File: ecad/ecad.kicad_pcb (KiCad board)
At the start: 4 copper layers, 130.5 x 110 mm, 101 parts, among them J1 JTAG, J2 USB_C, J3 Display, SW1 Kailh choc v2, SW10 RotaryEncoder_Switch, SW11 RotaryEncoder_Switch, SW12 Kailh choc v2, SW13 Kailh choc v2, SW14 Kailh choc v2, SW15 RESET, SW16 Kailh choc v2, SW17 Kailh choc v2, SW18 Kailh choc v2, SW19 Kailh choc v2, SW2 Kailh choc v2, SW20 Kailh choc v2, SW21 Kailh choc v2, SW22 Kailh choc v2, SW23 Kailh choc v2, SW24 Kailh choc v2, SW25 Kailh choc v2, SW3 Kailh choc v2, SW4 Kailh choc v2, SW5 Kailh choc v2, SW6 Kailh choc v2, SW7 Kailh choc v2, SW8 Kailh choc v2, SW9 Kailh choc v2, U1 AP2112K-3.3, U2 RP2040, U4 SN74LV1T34DBV, U5 W25Q128JVP, Y1 12MHz

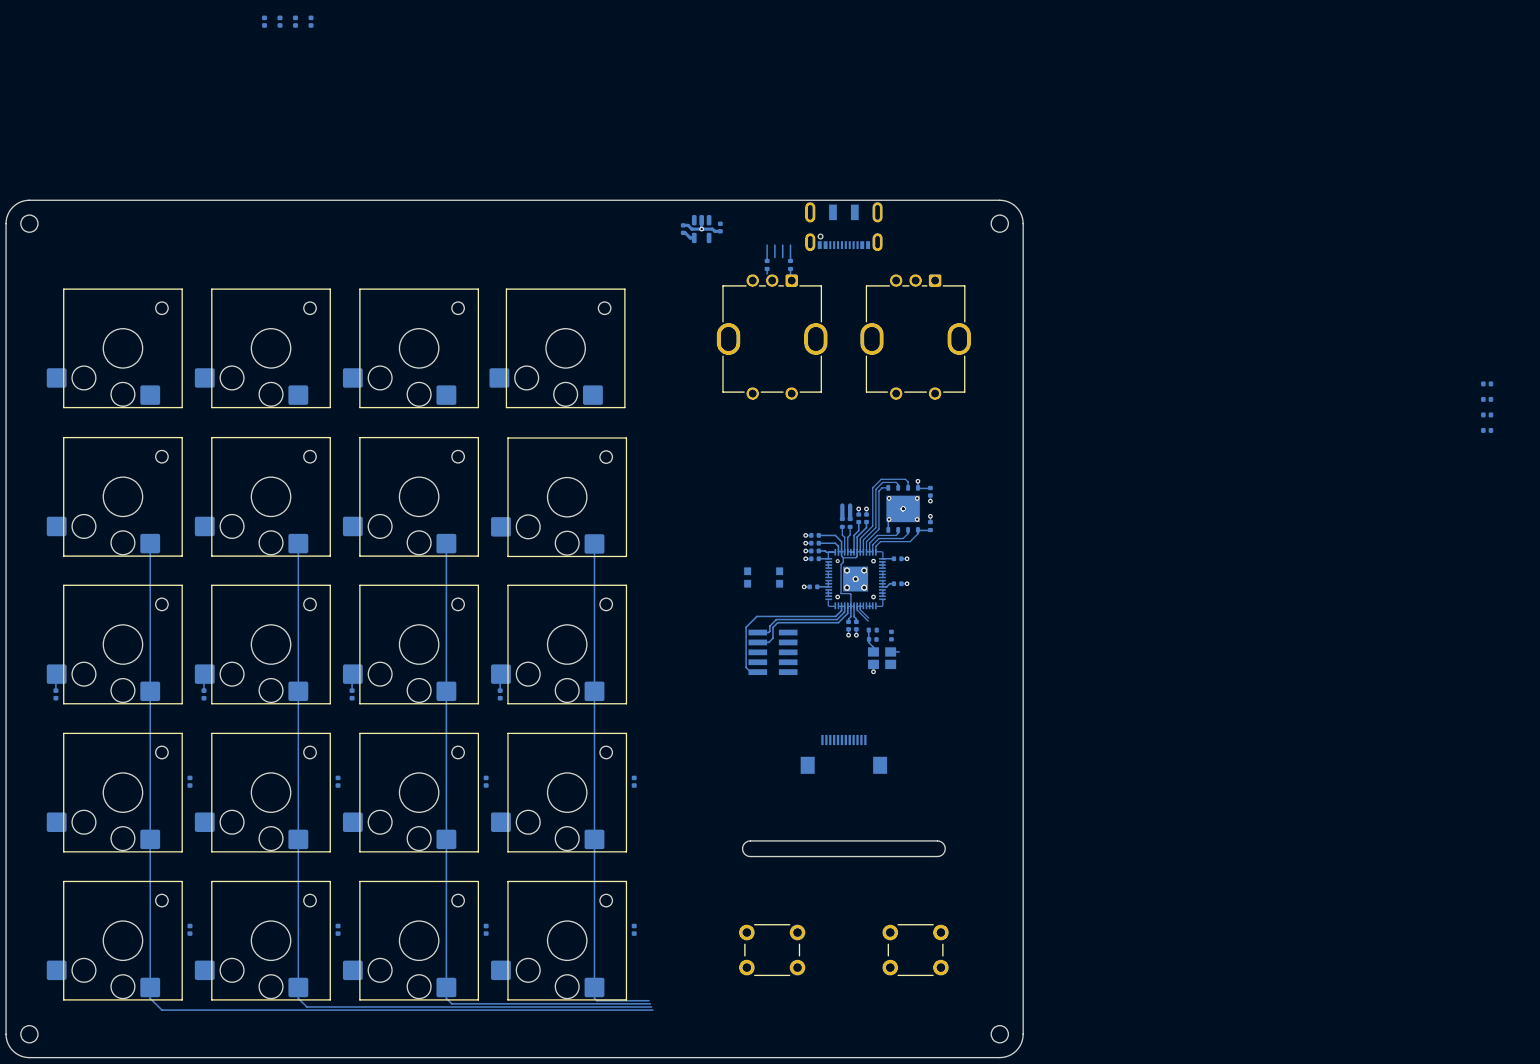
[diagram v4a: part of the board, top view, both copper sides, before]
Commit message: feat(ecad): hierarchical sheets, add switches net and change some components placement
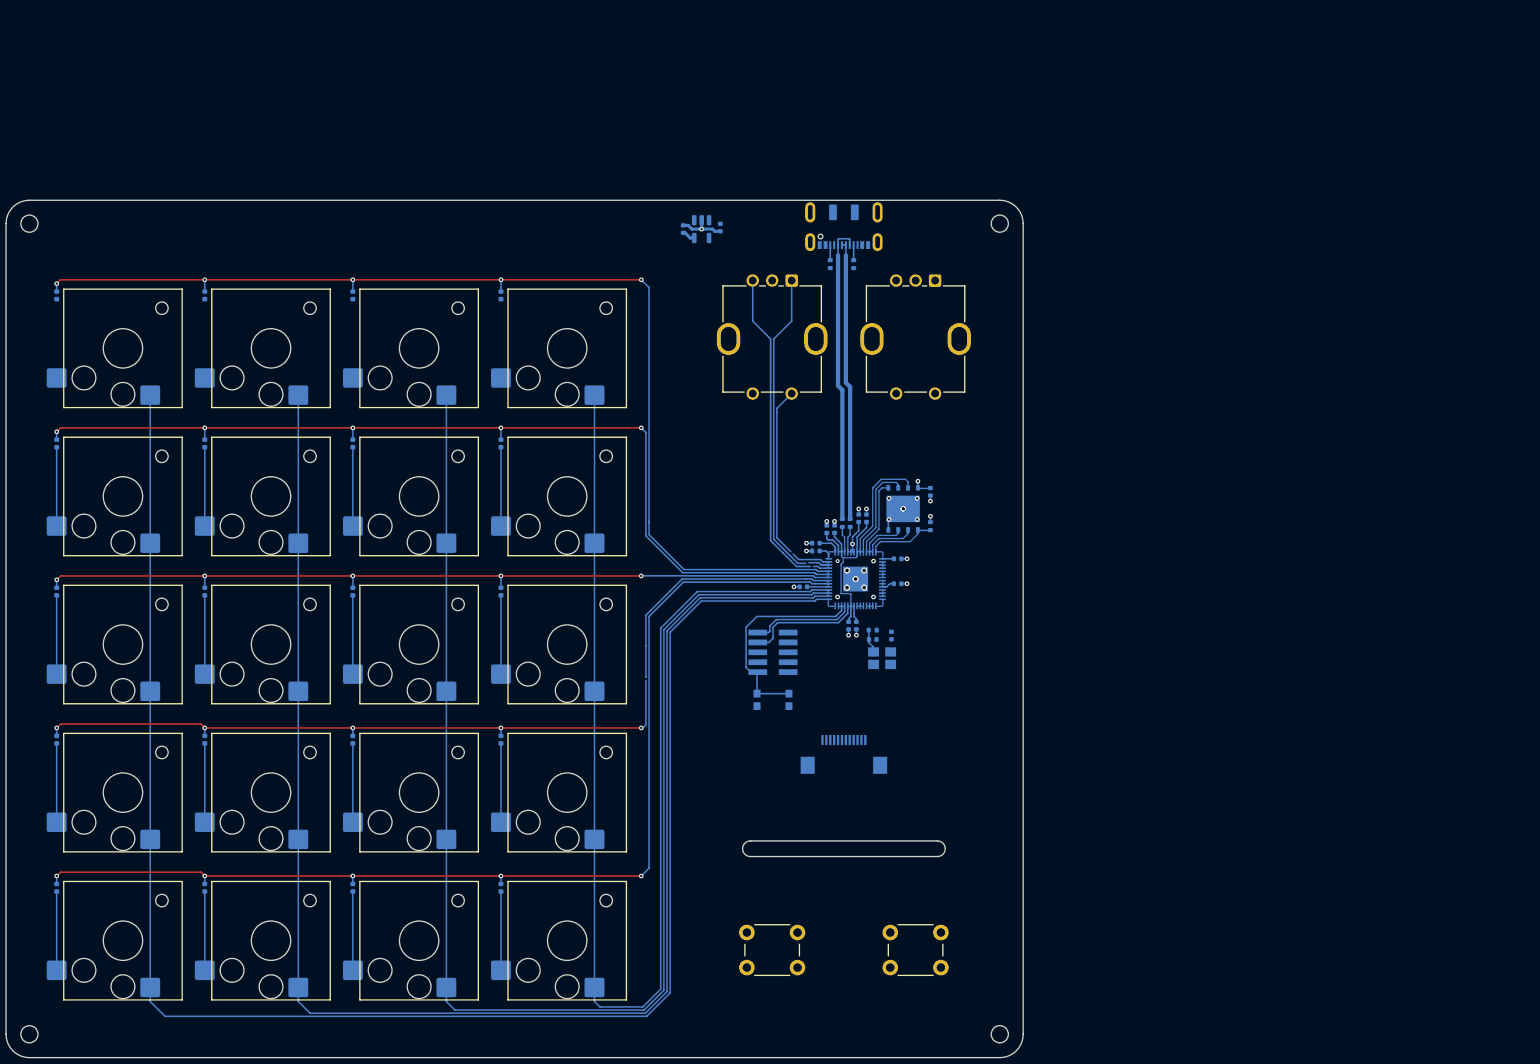
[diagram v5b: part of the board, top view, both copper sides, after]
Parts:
- moved D36 183.5 mm to (69.7, 99.1), turned to -90 degrees
- moved D35 164.6 mm to (88.7, 99.1), turned to -90 degrees
- moved D34 145.6 mm to (107.7, 99.1), turned to -90 degrees
- moved D33 126.8 mm to (126.7, 99.1), turned to -90 degrees
- moved D40 44.1 mm to (69.7, 80.1), turned to -90 degrees
- moved D37 42.7 mm to (126.7, 80.1), turned to -90 degrees
- moved D39 36.4 mm to (88.7, 80.1), turned to -90 degrees
- moved D38 35.9 mm to (107.7, 80.1), turned to -90 degrees
- moved D2 17.9 mm to (126.7, 137.1), turned to -90 degrees
- moved D3 17.9 mm to (126.7, 156.1), turned to -90 degrees
- moved D11 17.9 mm to (69.7, 137.1), turned to -90 degrees
- moved D12 17.9 mm to (69.7, 156.1), turned to -90 degrees
- moved D5 17.9 mm to (107.7, 137.1), turned to -90 degrees
- moved D6 17.9 mm to (107.7, 156.1), turned to -90 degrees
- moved D8 17.9 mm to (88.7, 137.1), turned to -90 degrees
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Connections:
- net /led/DIN renamed /Leds/DIN
- D1 pad 1: Net-(D1-K) -> /Switches/R3
- D10 pad 1: Net-(D1-K) -> /Switches/R3
- D11 pad 1: Net-(D11-K) -> /Switches/R4
- D12 pad 1: Net-(D12-K) -> /Switches/R5
- D2 pad 1: Net-(D11-K) -> /Switches/R4
- D3 pad 1: Net-(D12-K) -> /Switches/R5
- D33 pad 1: Net-(D33-K) -> /Switches/R2
- D34 pad 1: Net-(D33-K) -> /Switches/R2
- D35 pad 1: Net-(D33-K) -> /Switches/R2
- D36 pad 1: Net-(D33-K) -> /Switches/R2
- D37 pad 1: Net-(D37-K) -> /Switches/R1
- D38 pad 1: Net-(D37-K) -> /Switches/R1
- D39 pad 1: Net-(D37-K) -> /Switches/R1
- D4 pad 1: Net-(D1-K) -> /Switches/R3
- D40 pad 1: Net-(D37-K) -> /Switches/R1
- D5 pad 1: Net-(D11-K) -> /Switches/R4
- D6 pad 1: Net-(D12-K) -> /Switches/R5
- D7 pad 1: Net-(D1-K) -> /Switches/R3
- D8 pad 1: Net-(D11-K) -> /Switches/R4
- D9 pad 1: Net-(D12-K) -> /Switches/R5
- J3 pad 1: unconnected-(J3-Pin_1-Pad1) -> GND
- SW1 pad 1: Net-(U2-GPIO8) -> /Switches/C1
- SW12 pad 1: Net-(U2-GPIO11) -> /Switches/C4
- SW13 pad 1: Net-(U2-GPIO11) -> /Switches/C4
- SW14 pad 1: Net-(U2-GPIO11) -> /Switches/C4
- SW16 pad 1: Net-(U2-GPIO8) -> /Switches/C1
- SW17 pad 1: Net-(U2-GPIO9) -> /Switches/C2
- SW18 pad 1: Net-(U2-GPIO10) -> /Switches/C3
- SW19 pad 1: Net-(U2-GPIO11) -> /Switches/C4
- SW2 pad 1: Net-(U2-GPIO8) -> /Switches/C1
- SW20 pad 1: Net-(U2-GPIO8) -> /Switches/C1
- SW21 pad 1: Net-(U2-GPIO9) -> /Switches/C2
- SW22 pad 1: Net-(U2-GPIO10) -> /Switches/C3
- SW23 pad 1: Net-(U2-GPIO11) -> /Switches/C4
- SW3 pad 1: Net-(U2-GPIO8) -> /Switches/C1
- SW4 pad 1: Net-(U2-GPIO9) -> /Switches/C2
- SW5 pad 1: Net-(U2-GPIO9) -> /Switches/C2
- SW6 pad 1: Net-(U2-GPIO9) -> /Switches/C2
- SW7 pad 1: Net-(U2-GPIO10) -> /Switches/C3
- SW8 pad 1: Net-(U2-GPIO10) -> /Switches/C3
- SW9 pad 1: Net-(U2-GPIO10) -> /Switches/C3
- U2 pad 11: Net-(U2-GPIO8) -> unconnected-(U2-GPIO8-Pad11)
- U2 pad 12: Net-(U2-GPIO9) -> unconnected-(U2-GPIO9-Pad12)
- U2 pad 13: Net-(U2-GPIO10) -> unconnected-(U2-GPIO10-Pad13)
- U2 pad 14: Net-(U2-GPIO11) -> unconnected-(U2-GPIO11-Pad14)
- U2 pad 19: unconnected-(U2-TESTEN-Pad19) -> GND
- U2 pad 2: Net-(D33-K) -> unconnected-(U2-GPIO0-Pad2)
- U2 pad 29: unconnected-(U2-GPIO18-Pad29) -> /Switches/C4
- U2 pad 30: unconnected-(U2-GPIO19-Pad30) -> /Switches/C3
- U2 pad 31: unconnected-(U2-GPIO20-Pad31) -> /Switches/C2
- U2 pad 32: unconnected-(U2-GPIO21-Pad32) -> /Switches/C1
- U2 pad 34: unconnected-(U2-GPIO22-Pad34) -> /Switches/R5
- U2 pad 35: Net-(D1-K) -> /Switches/R4
- U2 pad 36: Net-(D11-K) -> /Switches/R3
- U2 pad 37: Net-(D12-K) -> /Switches/R2
- U2 pad 38: unconnected-(U2-GPIO26_ADC0-Pad38) -> /Switches/R1
- U2 pad 57: unconnected-(U2-GND-Pad57) -> GND
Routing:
- net /Switches/C4: track 0.00 -> 214.9 mm
- net /Switches/C3: track 0.00 -> 195.7 mm
- net /Switches/C2: track 0.00 -> 176.6 mm
- net /Switches/C1: track 0.00 -> 157.4 mm
- net /Switches/R1: track 0.00 -> 139.1 mm, vias 0 -> 5
- net /Switches/R5: track 0.00 -> 138.2 mm, vias 0 -> 5
- net Net-(U2-GPIO11): track 123.5 -> 0.00 mm
- net /Switches/R2: track 0.00 -> 120.4 mm, vias 0 -> 5
- net /Switches/R4: track 0.00 -> 119.4 mm, vias 0 -> 5
- net /Switches/R3: track 0.00 -> 104.9 mm, vias 0 -> 5
- net Net-(U2-GPIO10): track 104.1 -> 0.00 mm
- net Net-(U2-GPIO9): track 84.8 -> 0.00 mm
- net Net-(U2-GPIO8): track 65.4 -> 0.00 mm
- net unconnected-(SW11-PadB): track 0.00 -> 40.8 mm
- net unconnected-(SW11-PadA): track 0.00 -> 39.5 mm
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
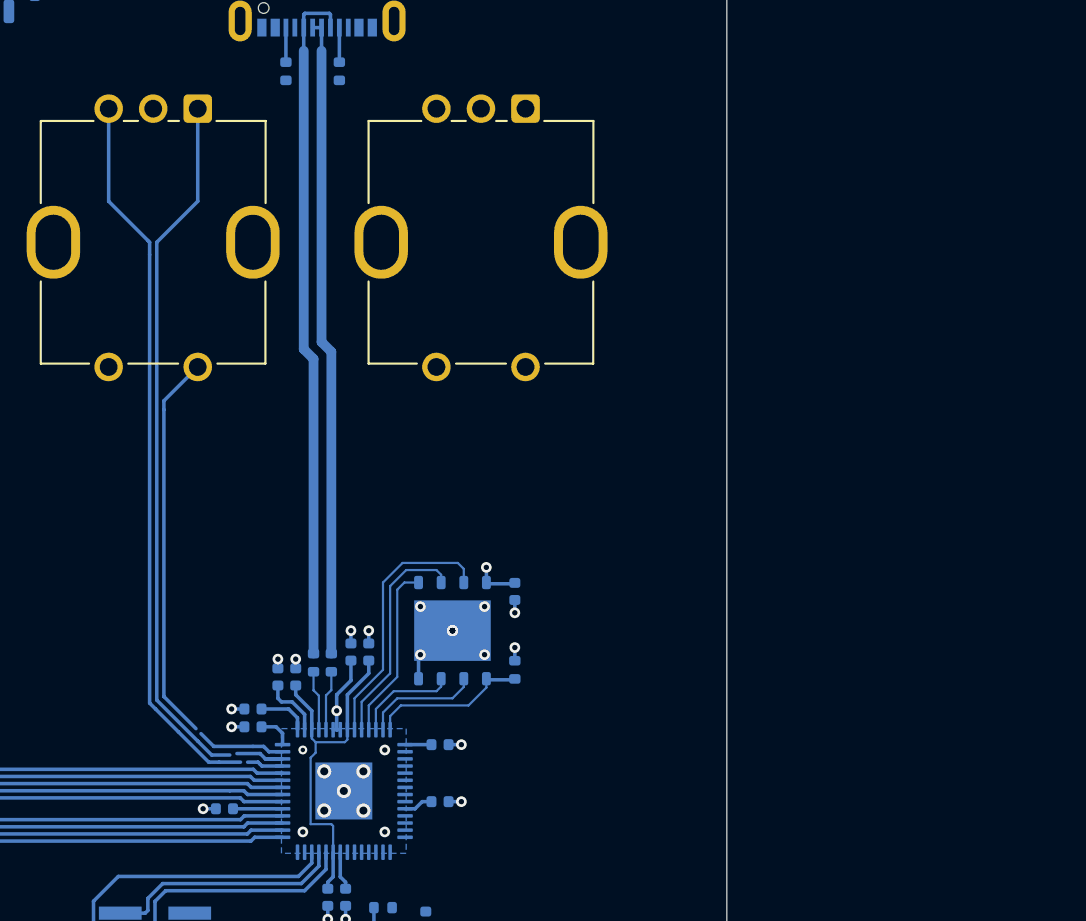
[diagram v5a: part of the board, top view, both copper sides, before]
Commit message: feat(ecad): route rotary encoders and change some pins arrangement
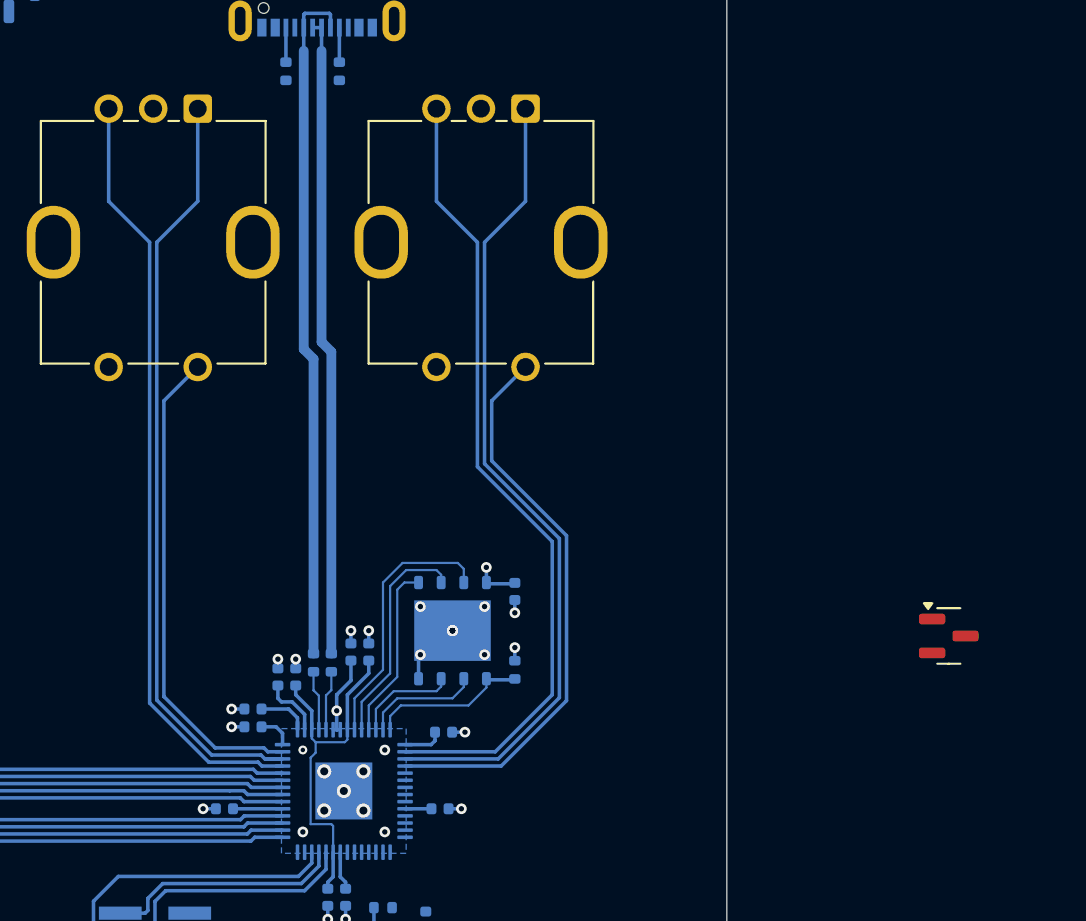
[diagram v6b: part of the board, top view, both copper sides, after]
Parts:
- added Q1: SS8050, Package_TO_SOT_SMD:SOT-23, F.Cu at (206.2, 107.8)
- moved C10 0.73 mm to (177.8, 113.2)
- moved C7 0.40 mm to (177.6, 117.5)
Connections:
- SW10 pad A: unconnected-(SW10-PadA) -> Net-(U2-GPIO1)
- SW10 pad B: unconnected-(SW10-PadB) -> Net-(U2-GPIO0)
- SW10 pad S1: unconnected-(SW10-PadS1) -> Net-(U2-GPIO2)
- SW11 pad A: unconnected-(SW11-PadA) -> Net-(U2-GPIO28)
- SW11 pad B: unconnected-(SW11-PadB) -> Net-(U2-GPIO27)
- SW11 pad S1: unconnected-(SW11-PadS1) -> Net-(U2-GPIO29)
- U2 pad 2: unconnected-(U2-GPIO0-Pad2) -> Net-(U2-GPIO0)
- U2 pad 3: unconnected-(U2-GPIO1-Pad3) -> Net-(U2-GPIO1)
- U2 pad 39: unconnected-(U2-GPIO27_ADC1-Pad39) -> Net-(U2-GPIO27)
- U2 pad 4: unconnected-(U2-GPIO2-Pad4) -> Net-(U2-GPIO2)
- U2 pad 40: unconnected-(U2-GPIO28_ADC2-Pad40) -> Net-(U2-GPIO28)
- U2 pad 41: unconnected-(U2-GPIO29_ADC3-Pad41) -> Net-(U2-GPIO29)
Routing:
- net Net-(U2-GPIO1): track 0.00 -> 45.8 mm
- net Net-(U2-GPIO0): track 0.00 -> 45.2 mm
- net Net-(U2-GPIO28): track 0.00 -> 43.5 mm
- net Net-(U2-GPIO27): track 0.00 -> 43.2 mm
- net unconnected-(SW11-PadB): track 40.8 -> 0.00 mm
- net unconnected-(SW11-PadA): track 39.5 -> 0.00 mm
- net Net-(U2-GPIO2): track 0.00 -> 31.8 mm
- net Net-(U2-GPIO29): track 0.00 -> 27.2 mm
- net unconnected-(SW11-PadS1): track 21.8 -> 0.00 mm
- net unconnected-(U2-GPIO29_ADC3-Pad41): track 5.00 -> 0.00 mm
- net unconnected-(U2-GPIO28_ADC2-Pad40): track 3.59 -> 0.00 mm
- net unconnected-(U2-GPIO27_ADC1-Pad39): track 2.05 -> 0.00 mm
- net +3.3V: track 26.4 -> 27.0 mm

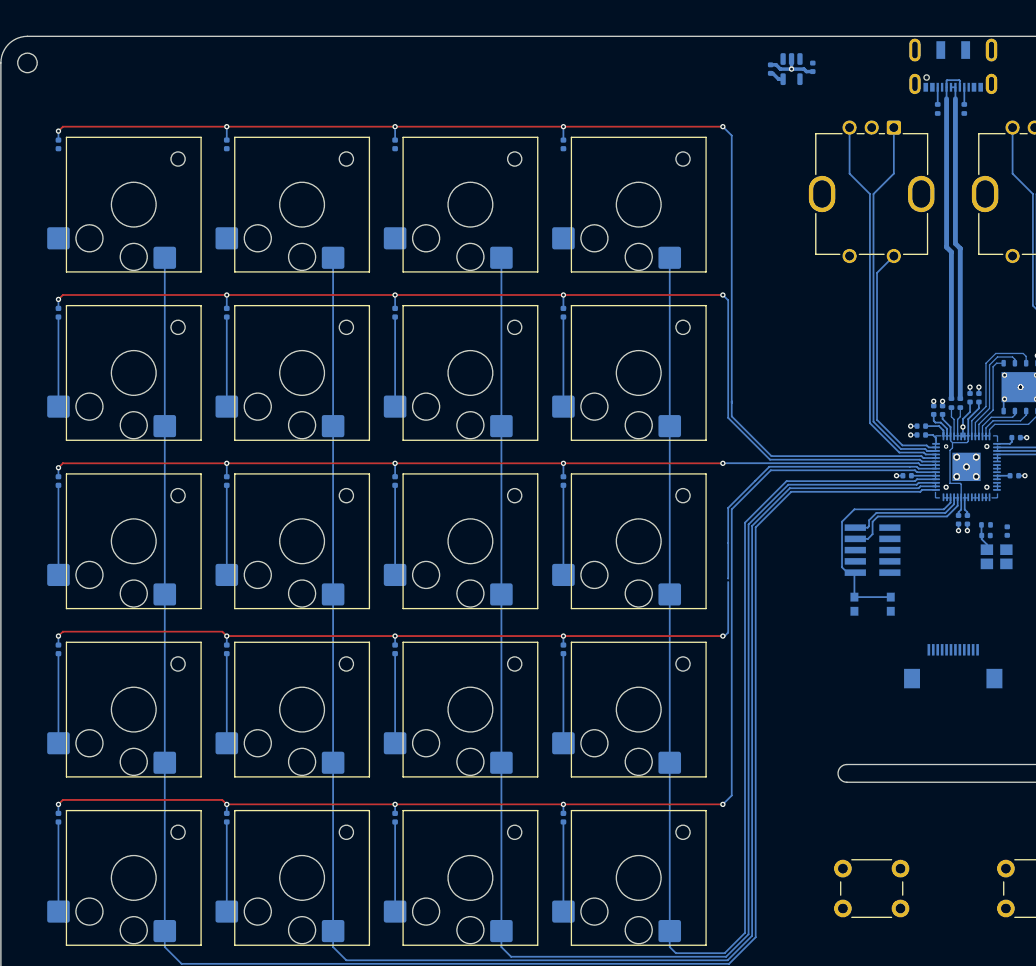
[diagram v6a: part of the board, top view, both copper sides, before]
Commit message: feat(ecad): change ref of swtiche diode and make the circuitry for the display
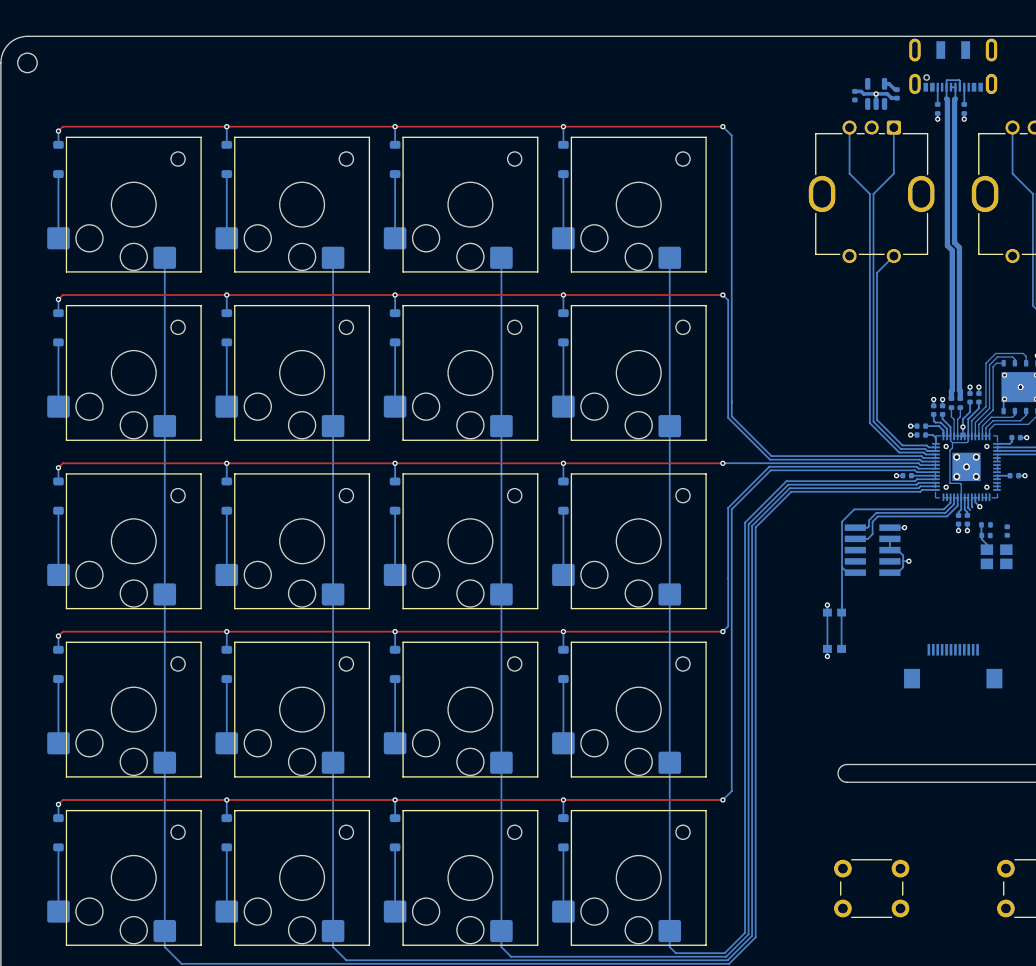
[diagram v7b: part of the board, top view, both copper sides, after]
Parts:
- D1, D10, D11, D12, D2, D3, D33, D34, D35, D36, D37, D38, D39, D4, D40, D5, D6, D7, D8, D9: value D_Small -> 1N4148W; footprint Diode_SMD:D_0402_1005Metric -> Diode_SMD:D_SOD-123
- moved C2 14.5 mm to (164.4, 74.4), turned to -90 degrees
- moved U1 9.95 mm to (162.0, 74.4), turned to 90 degrees
- moved C1 5.73 mm to (159.6, 74.6), turned to 90 degrees
- moved SW15 5.24 mm to (157.3, 135.0), turned to 90 degrees
- moved D11 1.70 mm to (69.7, 138.8)
- moved D12 1.70 mm to (69.7, 157.8)
- moved D2 1.70 mm to (126.7, 138.8)
- moved D3 1.70 mm to (126.7, 157.8)
- moved D5 1.70 mm to (107.7, 138.8)
- moved D6 1.70 mm to (107.7, 157.8)
- moved D8 1.70 mm to (88.7, 138.8)
- moved D9 1.70 mm to (88.7, 157.8)
- moved D1 1.70 mm to (126.7, 119.8)
- moved D10 1.70 mm to (69.7, 119.8)
- moved D33 1.70 mm to (126.7, 100.8)
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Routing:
- net GND: track 15.9 -> 31.6 mm, vias 28 -> 34
- net Net-(D40-A): track 0.00 -> 7.25 mm
- net Net-(D39-A): track 0.00 -> 7.25 mm
- net Net-(D38-A): track 0.00 -> 7.25 mm
- net Net-(D37-A): track 0.00 -> 7.25 mm
- net /Switches/R4: track 119.4 -> 122.6 mm
- net /Switches/R5: track 138.2 -> 141.1 mm
- net Net-(D7-A): track 10.3 -> 7.39 mm
- net Net-(D4-A): track 10.3 -> 7.39 mm
- net Net-(D1-A): track 10.3 -> 7.39 mm
- net Net-(D36-A): track 10.1 -> 7.25 mm
- net Net-(D35-A): track 10.1 -> 7.25 mm
- net Net-(D34-A): track 10.1 -> 7.25 mm
- net Net-(D33-A): track 10.1 -> 7.25 mm
- net Net-(D10-A): track 10.1 -> 7.25 mm
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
